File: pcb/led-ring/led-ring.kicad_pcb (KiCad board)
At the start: 2 copper layers, 30 x 30 mm, 31 parts, among them P1 CONN_01X12

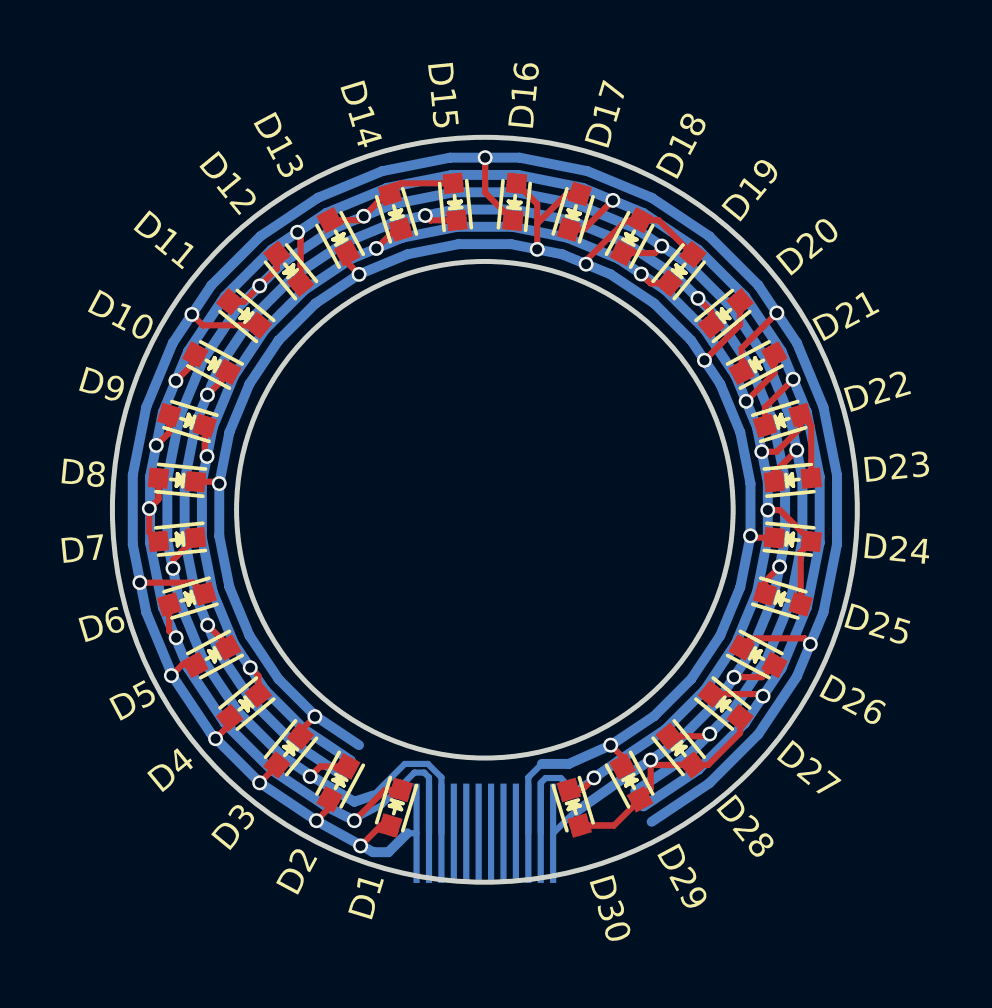
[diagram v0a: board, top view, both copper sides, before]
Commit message: o Move outer rings to top layer to avoid a couple of vias.
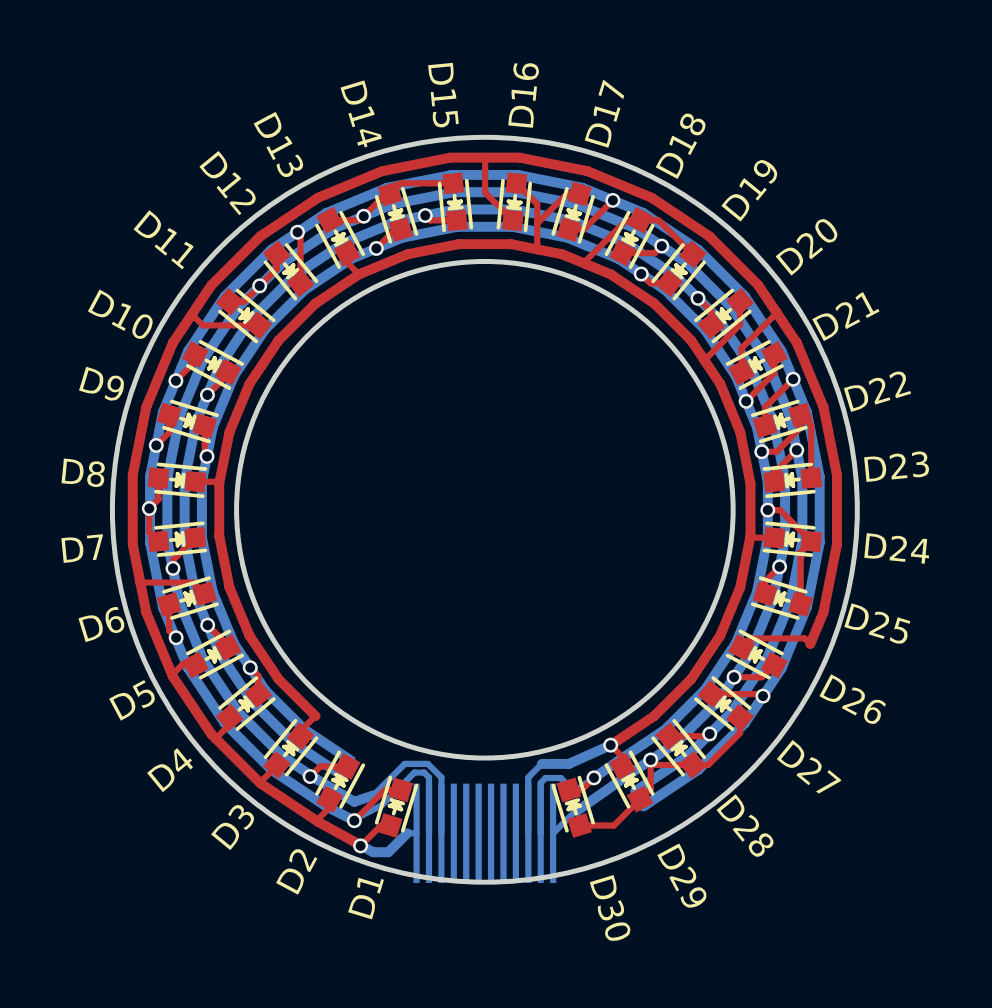
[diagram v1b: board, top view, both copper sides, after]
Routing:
- net A: track 100.7 -> 90.7 mm, vias 10 -> 1
- net D: track 81.8 -> 79.7 mm, vias 8 -> 1

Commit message: o Remove tail-traces - traces after the last via that uses them.
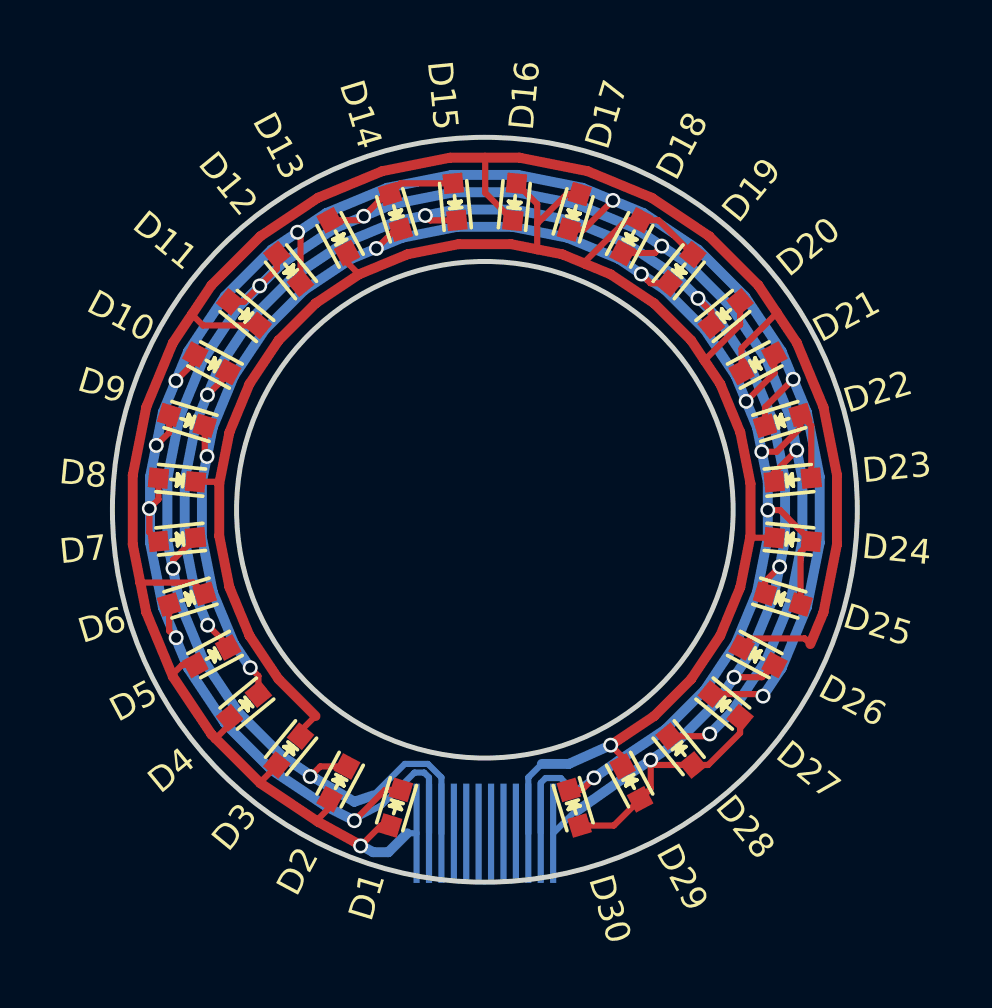
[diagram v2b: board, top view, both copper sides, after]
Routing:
- net F: track 85.9 -> 77.6 mm
- net B: track 97.5 -> 90.9 mm
- net E: track 85.6 -> 80.1 mm
- net C: track 92.4 -> 88.6 mm
